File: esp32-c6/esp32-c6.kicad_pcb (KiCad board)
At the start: 2 copper layers, 1 part, among them U1 ESP32-C6

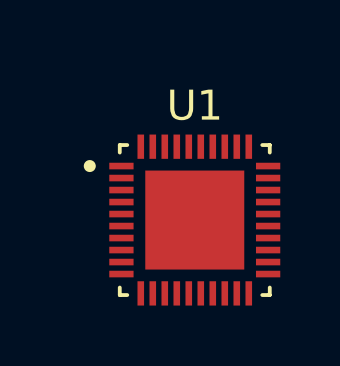
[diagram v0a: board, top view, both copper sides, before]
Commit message: fix: use official espressif lib for esp32-c6 projects
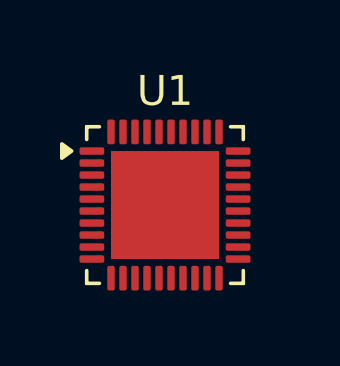
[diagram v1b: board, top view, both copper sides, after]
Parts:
- U1: footprint ESP32:ESP32-C6 -> Package_DFN_QFN:QFN-40-1EP_5x5mm_P0.4mm_EP3.6x3.6mm
- moved U1 1.11 mm to (149.1, 99.7)
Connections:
- net VDDA3P3 renamed Net-(U1-VDDA3P3-Pad2)
